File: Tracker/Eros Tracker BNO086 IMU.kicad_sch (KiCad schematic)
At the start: 7 parts, among them U3 BNO086

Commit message: Midway through board layout
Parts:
- C4: renamed from C5; footprint (none) -> Capacitor_SMD:C_0805_2012Metric; Manufacturer_Name (none) -> Samsung; Manufacturer_Part_Number (none) -> CL21B104MACNNNC; Mouser Part Number (none) -> 187-CL21B104MACNNNC; Mouser Price/Stock (none) -> https://www.mouser.com/ProductDetail/Samsung-Electro-Mechan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
- C5: renamed from C3; footprint (none) -> Capacitor_SMD:C_0805_2012Metric; Manufacturer_Name (none) -> Samsung; Manufacturer_Part_Number (none) -> CL21B104MACNNNC; Mouser Part Number (none) -> 187-CL21B104MACNNNC; Mouser Price/Stock (none) -> https://www.mouser.com/ProductDetail/Samsung-Electro-Mechan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
- C6: renamed from C4; footprint (none) -> Capacitor_SMD:C_0805_2012Metric; Manufacturer_Name (none) -> Samsung; Manufacturer_Part_Number (none) -> CL21B104MACNNNC; Mouser Part Number (none) -> 187-CL21B104MACNNNC; Mouser Price/Stock (none) -> https://www.mouser.com/ProductDetail/Samsung-Electro-Mechan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
- R19: renamed from R10; value 10k -> 10k 1%; footprint (none) -> Resistor_SMD:R_0805_2012Metric; Manufacturer_Name (none) -> YAGEO; Manufacturer_Part_Number (none) -> RT0805FRE0710KL; Mouser Part Number (none) -> 603-RT0805FRE0710KL; Mouser Price/Stock (none) -> https://www.mouser.com/ProductDetail/YAGEO/RT0805FRE0710KL?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
- R20: renamed from R11; footprint (none) -> Resistor_SMD:R_0805_2012Metric; Manufacturer_Name (none) -> YAGEO; Manufacturer_Part_Number (none) -> RT0805FRE132K2L; Mouser Part Number (none) -> 603-RT0805FRE132K2L; Mouser Price/Stock (none) -> https://www.mouser.com/ProductDetail/YAGEO/RT0805FRE132K2L?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
- R21: renamed from R12; footprint (none) -> Resistor_SMD:R_0805_2012Metric; Manufacturer_Name (none) -> YAGEO; Manufacturer_Part_Number (none) -> RT0805FRE132K2L; Mouser Part Number (none) -> 603-RT0805FRE132K2L; Mouser Price/Stock (none) -> https://www.mouser.com/ProductDetail/YAGEO/RT0805FRE132K2L?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
- U4: renamed from U3; DigiKey Part Number (none) -> 1888-BNO086CT-ND; DigiKey Price/Stock (none) -> https://www.digikey.com/en/products/detail/ceva-technologie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; Manufacturer_Name (none) -> CEVA Technologies; Manufacturer_Part_Number (none) -> BNO086
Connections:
- no-connect marks 1 -> 2

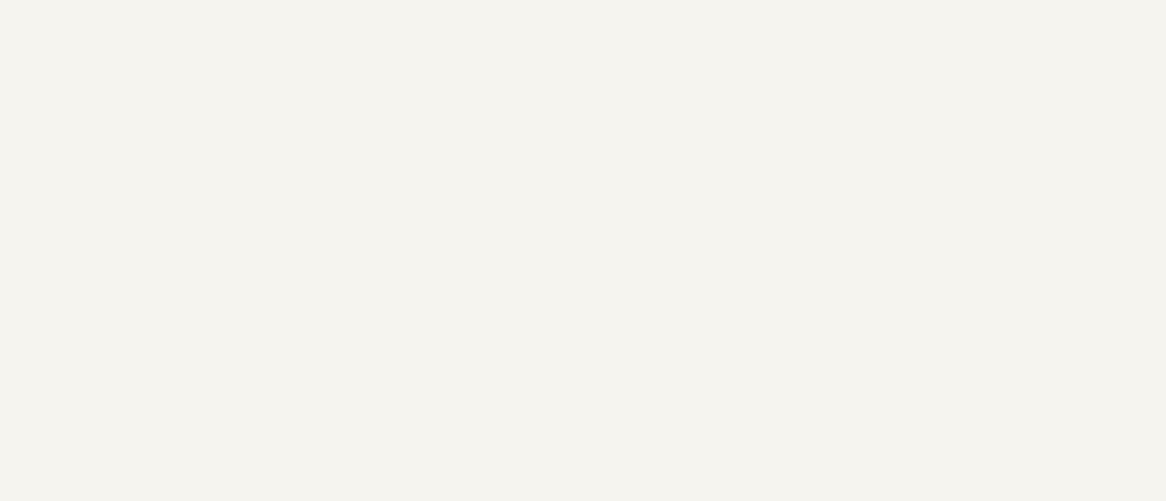
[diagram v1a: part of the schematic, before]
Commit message: Added cuts and jumps for Rev A
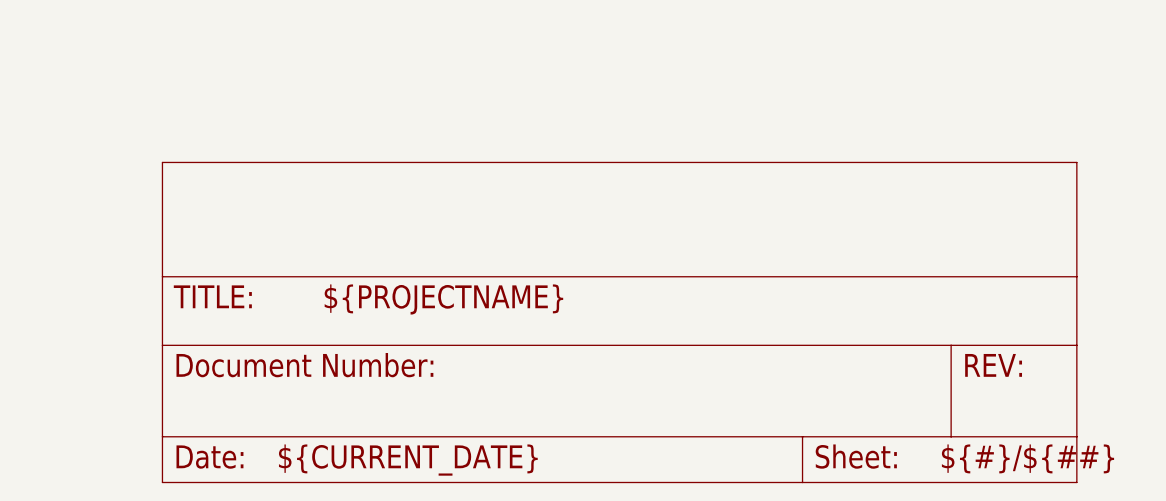
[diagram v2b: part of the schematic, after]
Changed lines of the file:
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@@
+    )
+  )
+  (symbol (lib_id "Eros Tracker-eagle-import:FRAME_A_L") (at 194.31 209.55 0) (unit 2)
+    (in_bom yes) (on_board yes) (dnp no)
+    (property "Reference" "#FRAME1" (at 194.31 209.55 0)
+      (effects (font (size 1.27 1.27)) hide)
+    )
+    (property "Value" "FRAME_A_L" (at 194.31 209.55 0)
+      (effects (font (size 1.27 1.27)) hide)
+    )
+    (property "Footprint" "" (at 194.31 209.55 0)
+      (effects (font (size 1.27 1.27)) hide)
+    )
+    (property "Datasheet" "" (at 194.31 209.55 0)
+      (effects (font (size 1.27 1.27)) hide)
+    )
+    (instances
+      (project "Eros Tracker"
+        (path "/e762b1f0-85b9-427f-b9a8-4b9d5ef7d00a/9c812c5a-2871-41e5-a7a0-ff8823ff9651"
+          (reference "#FRAME1") (unit 2)
+        )
+        (path "/e762b1f0-85b9-427f-b9a8-4b9d5ef7d00a/2a7cc5d7-0983-4896-a61d-6a51fe429227"
+          (reference "#FRAME3") (unit 2)
+        )
+      )
     )
   )
@@
       (effects (font (size 1.27 1.27)) hide)
     )
-    (property "Datasheet" "https://www.mouser.com/datasheet/2/447/PYu_RT_1_to_0_01_RoHS_L_12-3003070.pdf" (at 177.8 93.98 0)
+    (property "Datasheet" "~" (at 177.8 93.98 0)
       (effects (font (size 1.27 1.27)) hide)
     )
@@
       (effects (font (size 1.27 1.27)) hide)
     )
-    (property "Datasheet" "https://www.mouser.com/datasheet/2/585/MLCC-1837944.pdf" (at 168.91 116.84 0)
+    (property "Datasheet" "~" (at 168.91 116.84 0)
       (effects (font (size 1.27 1.27)) hide)
     )
@@
       (effects (font (size 1.27 1.27)) hide)
     )
-    (property "Datasheet" "https://www.mouser.com/datasheet/2/585/MLCC-1837944.pdf" (at 118.11 26.67 0)
+    (property "Datasheet" "~" (at 118.11 26.67 0)
       (effects (font (size 1.27 1.27)) hide)
     )
@@
       (effects (font (size 1.27 1.27)) hide)
     )
-    (property "Datasheet" "https://www.mouser.com/datasheet/2/585/MLCC-1837944.pdf" (at 128.27 26.67 0)
+    (property "Datasheet" "~" (at 128.27 26.67 0)
       (effects (font (size 1.27 1.27)) hide)
     )
@@
       (effects (font (size 1.27 1.27)) hide)
     )
-    (property "Datasheet" "https://www.mouser.com/datasheet/2/447/PYu_RT_1_to_0_01_RoHS_L_12-3003070.pdf" (at 87.63 93.98 0)
+    (property "Datasheet" "~" (at 87.63 93.98 0)
       (effects (font (size 1.27 1.27)) hide)
     )
@@
       (effects (font (size 1.27 1.27)) hide)
     )
-    (property "Datasheet" "https://www.mouser.com/datasheet/2/447/PYu_RT_1_to_0_01_RoHS_L_12-3003070.pdf" (at 189.23 93.98 0)
-      (effects (font (size 1.27 1.27)) hide)
-    )
+    (property "Datasheet" "~" (at 189.23 93.98 0)
+      (effects (font (size 1.27 1.27)) hide)
+    )

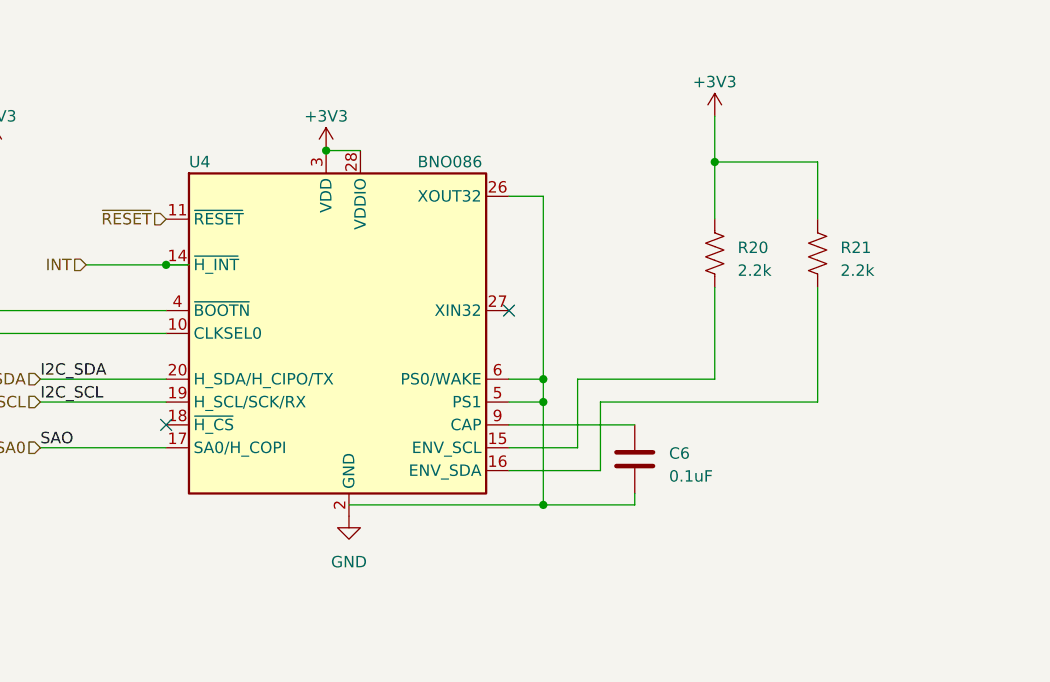
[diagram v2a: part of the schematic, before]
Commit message: RevC release. Power passthrough, battery voltage monitoring, IMU interrupt line fixed. TVS diodes added to all human-reachable connections.
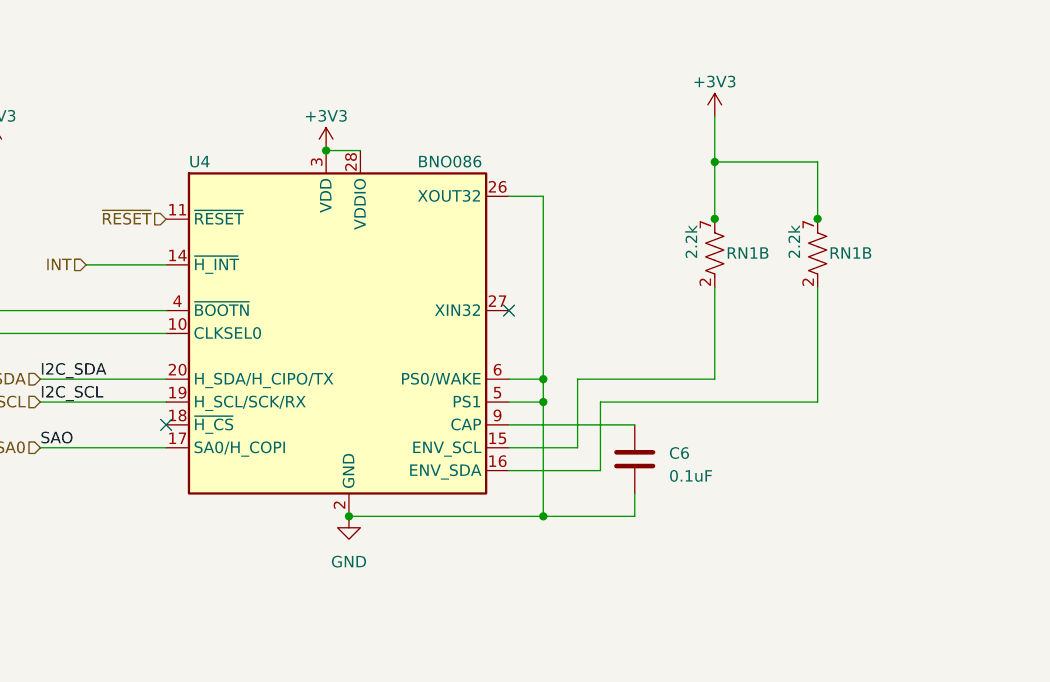
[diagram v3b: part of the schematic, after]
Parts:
- removed R20, R21: 2.2k, Resistor_SMD:R_0805_2012Metric, symbol Device:R_US
- added RN1 (x2): 2.2k, Eros Tracker:CAY10-xxxJ4, symbol Eros Tracker:CAY10-xxxJ4
- C4, C5, C6: footprint Capacitor_SMD:C_0805_2012Metric -> Capacitor_SMD:C_0402_1005Metric; Manufacturer_Part_Number CL21B104MACNNNC -> CL05B104KA5NNNC; Mouser Part Number 187-CL21B104MACNNNC -> 187-CL05B104KA5NNNC; Mouser Price/Stock https://www.mouser.com/ProductDetail/Samsung-Electro-Mechanics/CL21B104MACNNNC?qs=xZ%2FP%252Ba9zWqbIolF6La19LA%3D%3D -> https://www.mouser.com/ProductDetail/Samsung-Electro-Mechanics/CL05B104KA5NNNC?qs=Efv9o2T6U88DLyyMSzjXSQ%3D%3D
- R19: footprint Resistor_SMD:R_0805_2012Metric -> Resistor_SMD:R_0402_1005Metric; Manufacturer_Part_Number RT0805FRE0710KL -> RT0402FRE0710KL; Mouser Part Number 603-RT0805FRE0710KL -> 603-RT0402FRE0710KL; Mouser Price/Stock https://www.mouser.com/ProductDetail/YAGEO/RT0805FRE0710KL?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 -> https://www.mouser.com/ProductDetail/YAGEO/RT0402FRE0710KL?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
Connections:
- net +3V3: now also RN1.7, RN1.7
- net GND: now also C6.2, U4.26 (XOUT32), U4.5 (PS1), U4.6 (PS0/WAKE)
- net at U4.15 (ENV_SCL): now also RN1.2
- net at U4.16 (ENV_SDA): now also RN1.2
